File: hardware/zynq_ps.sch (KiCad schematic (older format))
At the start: 26 parts, among them J1401 DM3CS, SW1401 SW_Push, U1 xc7z030sbg485, U1401 CAT24C02TDI-GT3, U1402 EMIF06-MSD02N16, U1404 33.333MHZ

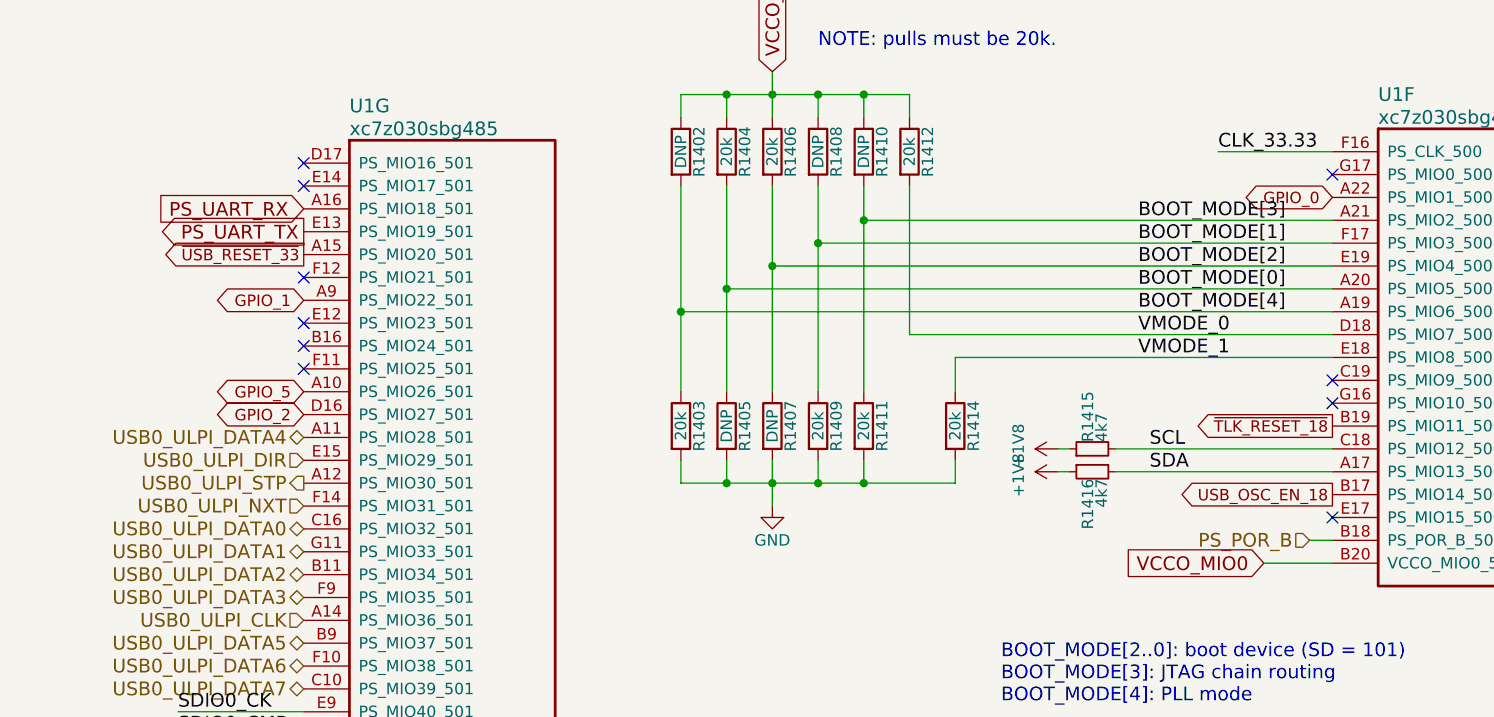
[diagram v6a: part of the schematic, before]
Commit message: First Version without any Net not routed.
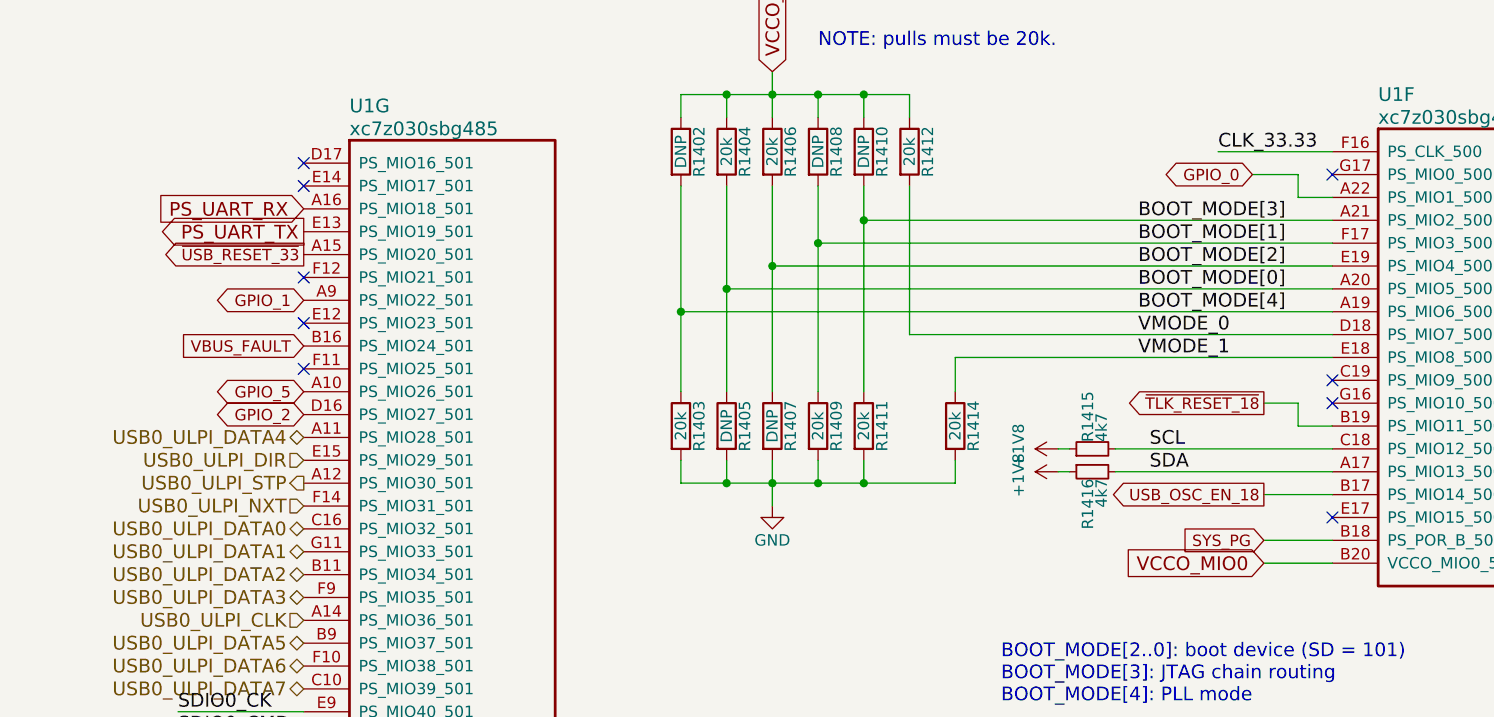
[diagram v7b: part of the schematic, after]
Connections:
- net VBUS_FAULT: now reaches U1.B16 (PS_MIO24_501)
- net PS_POR_B renamed SYS_PG
- no-connect marks 15 -> 14
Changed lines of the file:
@@
 $Descr A4 11693 8268
 encoding utf-8
-Sheet 14 21
+Sheet 20 21
 Title ""
 Date ""
@@
 F 7 "1" H 10000 1400 50  0001 C CNN "Populate for CLG484(Z-7012s/Z-7015)"
 	6    10000 1400
-	1    0    0    -1
-$EndComp
-$Comp
-L xilinx_zynq_clg485:xc7z030sbg485 U1
-U 7 1 596E7E6B
-P 5500 1450
-F 0 "U1" H 5700 1700 60  0000 L CNN
-F 1 "xc7z030sbg485" H 5700 1600 60  0000 L CNN
-F 2 "footprints:SBG485_22x22_19.0x19.0mm_Pitch0.8mm" H 5500 1450 60  0001 C CNN
-F 3 "" H 5500 1450 60  0001 C CNN
-F 4 "1" H 5500 1450 50  0001 C CNN "Populated"
-F 5 "SPEC" H 5500 1450 50  0001 C CNN "Source"
-F 6 "1" H 5500 1450 50  0001 C CNN "Populate for SBGA485(Z-7030)"
-F 7 "1" H 5500 1450 50  0001 C CNN "Populate for CLG484(Z-7012s/Z-7015)"
-	7    5500 1450
 	1    0    0    -1
 $EndComp
@@
 	0    -1   -1   0
 $EndComp
-Wire Wire Line
-	9900 3100 10000 3100
 Text Label 4950 5350 0    60   ~ 0
 PS_RESET
-Text HLabel 9900 3100 0    60   Input ~ 0
-PS_POR_B
 Text GLabel 7550 1050 1    60   Input ~ 0
 VCCO_MIO0
@@
 Text GLabel 5500 1850 0    50   Output ~ 0
 ~USB_RESET_33~
-Text GLabel 10000 2600 0    50   Output ~ 0
+Text GLabel 9700 2500 0    50   Output ~ 0
 ~TLK_RESET_18~
 Text GLabel 5500 4850 0    50   Output ~ 0
@@
 	8350 2300 8350 2450
 NoConn ~ 9150 5600
-Text GLabel 10000 2900 0    50   Output ~ 0
+Text GLabel 9700 2900 0    50   Output ~ 0
 USB_OSC_EN_18
 NoConn ~ 5500 1450
@@
 	1    0    0    -1
 $EndComp
-Text GLabel 10000 1600 0    50   BiDi ~ 0
+Text GLabel 9650 1500 0    50   BiDi ~ 0
 GPIO_0
 Text GLabel 5500 2550 0    50   BiDi ~ 0
@@
 GPIO_4
 NoConn ~ 5500 2150
-NoConn ~ 5500 2250
 NoConn ~ 10000 3000
+Text GLabel 9700 3100 0    50   Input ~ 0
+SYS_PG
+Wire Wire Line
+	9700 3100 10000 3100
+Wire Wire Line
+	9700 2900 10000 2900
+Wire Wire Line
+	9700 2500 9850 2500
+Wire Wire Line
+	9850 2500 9850 2600
+Wire Wire Line
+	9850 2600 10000 2600
+Wire Wire Line
+	9650 1500 9850 1500
+Wire Wire Line
+	9850 1500 9850 1600
+Wire Wire Line
+	9850 1600 10000 1600
+Text GLabel 5500 2250 0    50   Input ~ 0
+VBUS_FAULT
+$Comp
+L xilinx_zynq_clg485:xc7z030sbg485 U1
+U 7 1 596E7E6B
+P 5500 1450
+F 0 "U1" H 5700 1700 60  0000 L CNN
+F 1 "xc7z030sbg485" H 5700 1600 60  0000 L CNN
+F 2 "footprints:SBG485_22x22_19.0x19.0mm_Pitch0.8mm" H 5500 1450 60  0001 C CNN
+F 3 "" H 5500 1450 60  0001 C CNN
+F 4 "1" H 5500 1450 50  0001 C CNN "Populated"
+F 5 "SPEC" H 5500 1450 50  0001 C CNN "Source"
+F 6 "1" H 5500 1450 50  0001 C CNN "Populate for SBGA485(Z-7030)"
+F 7 "1" H 5500 1450 50  0001 C CNN "Populate for CLG484(Z-7012s/Z-7015)"
+	7    5500 1450
+	1    0    0    -1
+$EndComp
 $EndSCHEMATC

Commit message: Added Step Models, fixed some footprints(e.g. added solderpaste), cleaned up a bit
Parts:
- U1: footprint footprints:SBG485_22x22_19.0x19.0mm_Pitch0.8mm -> footprints:Xilinx_SBG485_22x22_19.0x19.0mm_Pitch0.8mm
- U1404: footprint footprints:ASDMB_2.5x2.0mm_1.65mm_pitch -> footprints:Y_ASDMB_2.5x2.0mm_1.65mm_pitch
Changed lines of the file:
@@
 EESchema Schematic File Version 4
 LIBS:zynq_board-cache
-EELAYER 26 0
+EELAYER 29 0
 EELAYER END
 $Descr A4 11693 8268
@@
 F 0 "U1" H 10200 1650 60  0000 L CNN
 F 1 "xc7z030sbg485" H 10200 1550 60  0000 L CNN
-F 2 "footprints:SBG485_22x22_19.0x19.0mm_Pitch0.8mm" H 10000 1400 60  0001 C CNN
+F 2 "footprints:Xilinx_SBG485_22x22_19.0x19.0mm_Pitch0.8mm" H 10000 1400 60  0001 C CNN
 F 3 "" H 10000 1400 60  0001 C CNN
 F 4 "1" H 10000 1400 50  0001 C CNN "Populated"
@@
 F 0 "U1404" H 9650 5650 60  0000 C CNN
 F 1 "33.333MHZ" H 9650 5750 60  0000 C CNN
-F 2 "footprints:ASDMB_2.5x2.0mm_1.65mm_pitch" H 9650 5700 60  0001 C CNN
+F 2 "footprints:Y_ASDMB_2.5x2.0mm_1.65mm_pitch" H 9650 5700 60  0001 C CNN
 F 3 "https://abracon.com/Oscillators/ASDMB.pdf" H 9650 5700 60  0001 C CNN
 F 4 "Abracon LLC" H 9650 5700 60  0001 C CNN "MFG Name"
@@
 F 0 "U1" H 5700 1700 60  0000 L CNN
 F 1 "xc7z030sbg485" H 5700 1600 60  0000 L CNN
-F 2 "footprints:SBG485_22x22_19.0x19.0mm_Pitch0.8mm" H 5500 1450 60  0001 C CNN
+F 2 "footprints:Xilinx_SBG485_22x22_19.0x19.0mm_Pitch0.8mm" H 5500 1450 60  0001 C CNN
 F 3 "" H 5500 1450 60  0001 C CNN
 F 4 "1" H 5500 1450 50  0001 C CNN "Populated"
